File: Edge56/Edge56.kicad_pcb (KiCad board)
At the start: 2 copper layers, 36.2 x 141 mm, 15 parts, among them J1 Conn_02x04_Top_Bottom, J10 Conn_01x28_Female, J11 Conn_01x28_Female, J12 Conn_02x04_Top_Bottom, J13 Conn_02x04_Top_Bottom, J14 Conn_02x04_Top_Bottom, J15 Conn_02x04_Top_Bottom, J2 Conn_02x04_Top_Bottom, J3 Conn_01x28_Female, J4 Conn_01x28_Female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

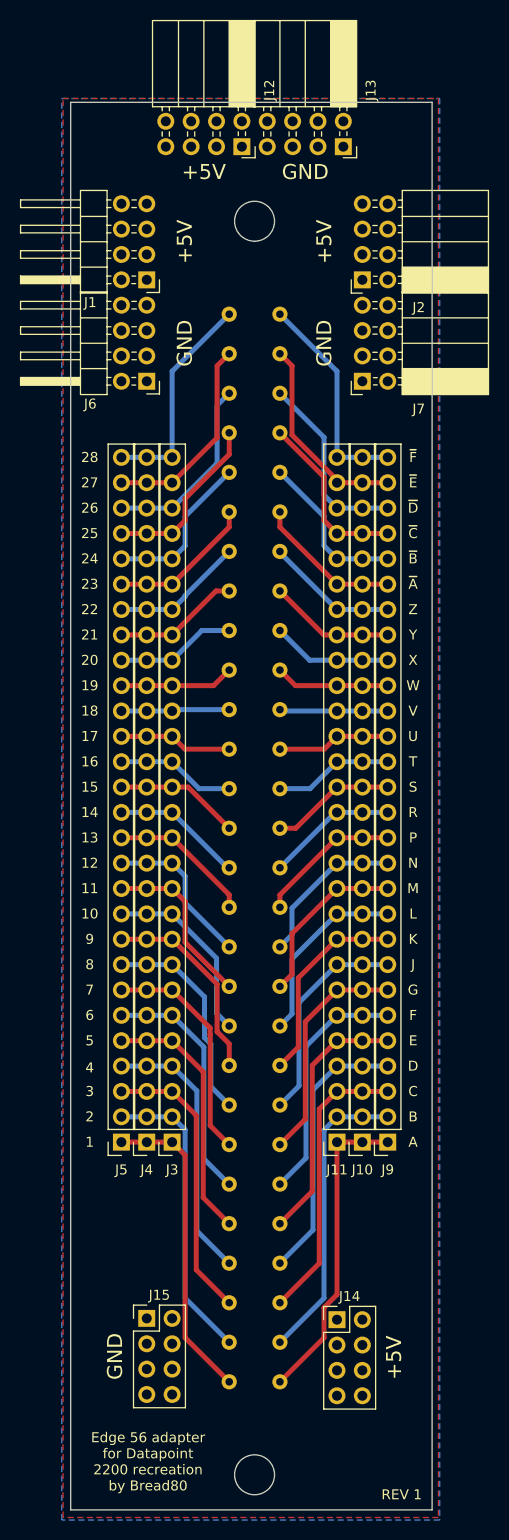
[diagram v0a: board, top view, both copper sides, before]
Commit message: Schematics for display & keyboard, adding LEDs to processor PCB
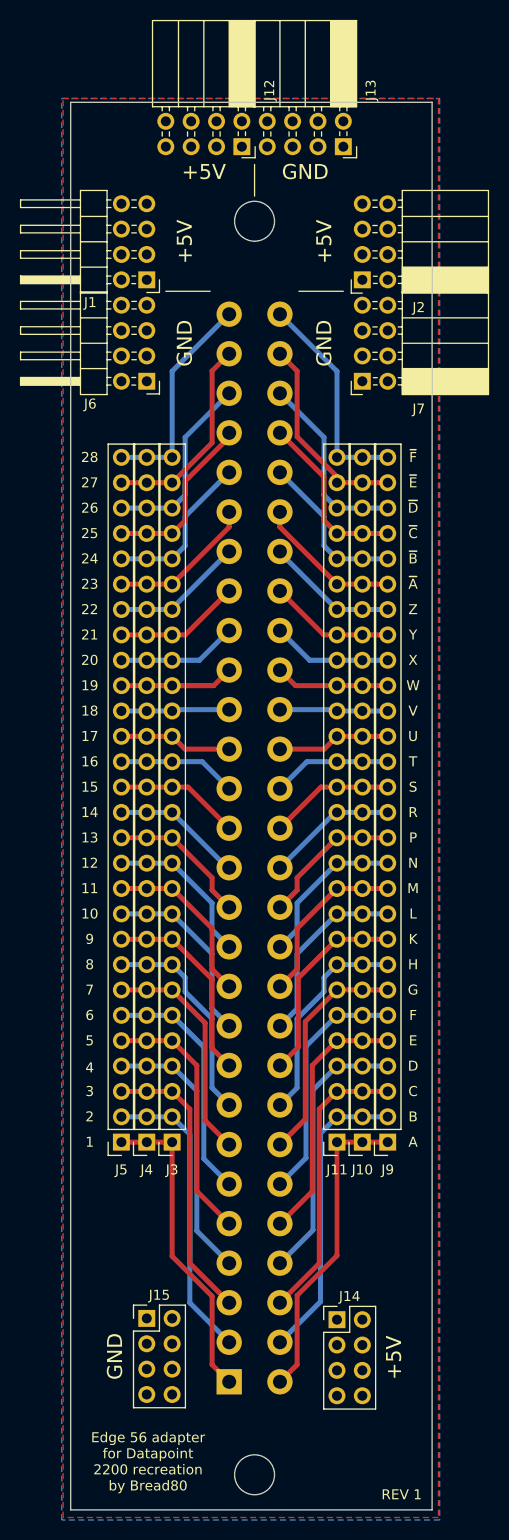
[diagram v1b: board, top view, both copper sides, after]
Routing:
- net Net-(J3-Pad19): track 12.6 -> 16.7 mm
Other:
- board text added: "H"
- board text removed: "J"
